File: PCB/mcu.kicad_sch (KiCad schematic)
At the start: 38 parts, among them J2 Conn_Coaxial, J3 Conn_Coaxial, SW2 PTS645VH58-2 LFS, SW3 TS04-66-50-BK-160-SMT, U24 RP2354B, U25 W25Q128JVS, Y1 ABM8AIG-12.000MHZ-12-2Z-T3

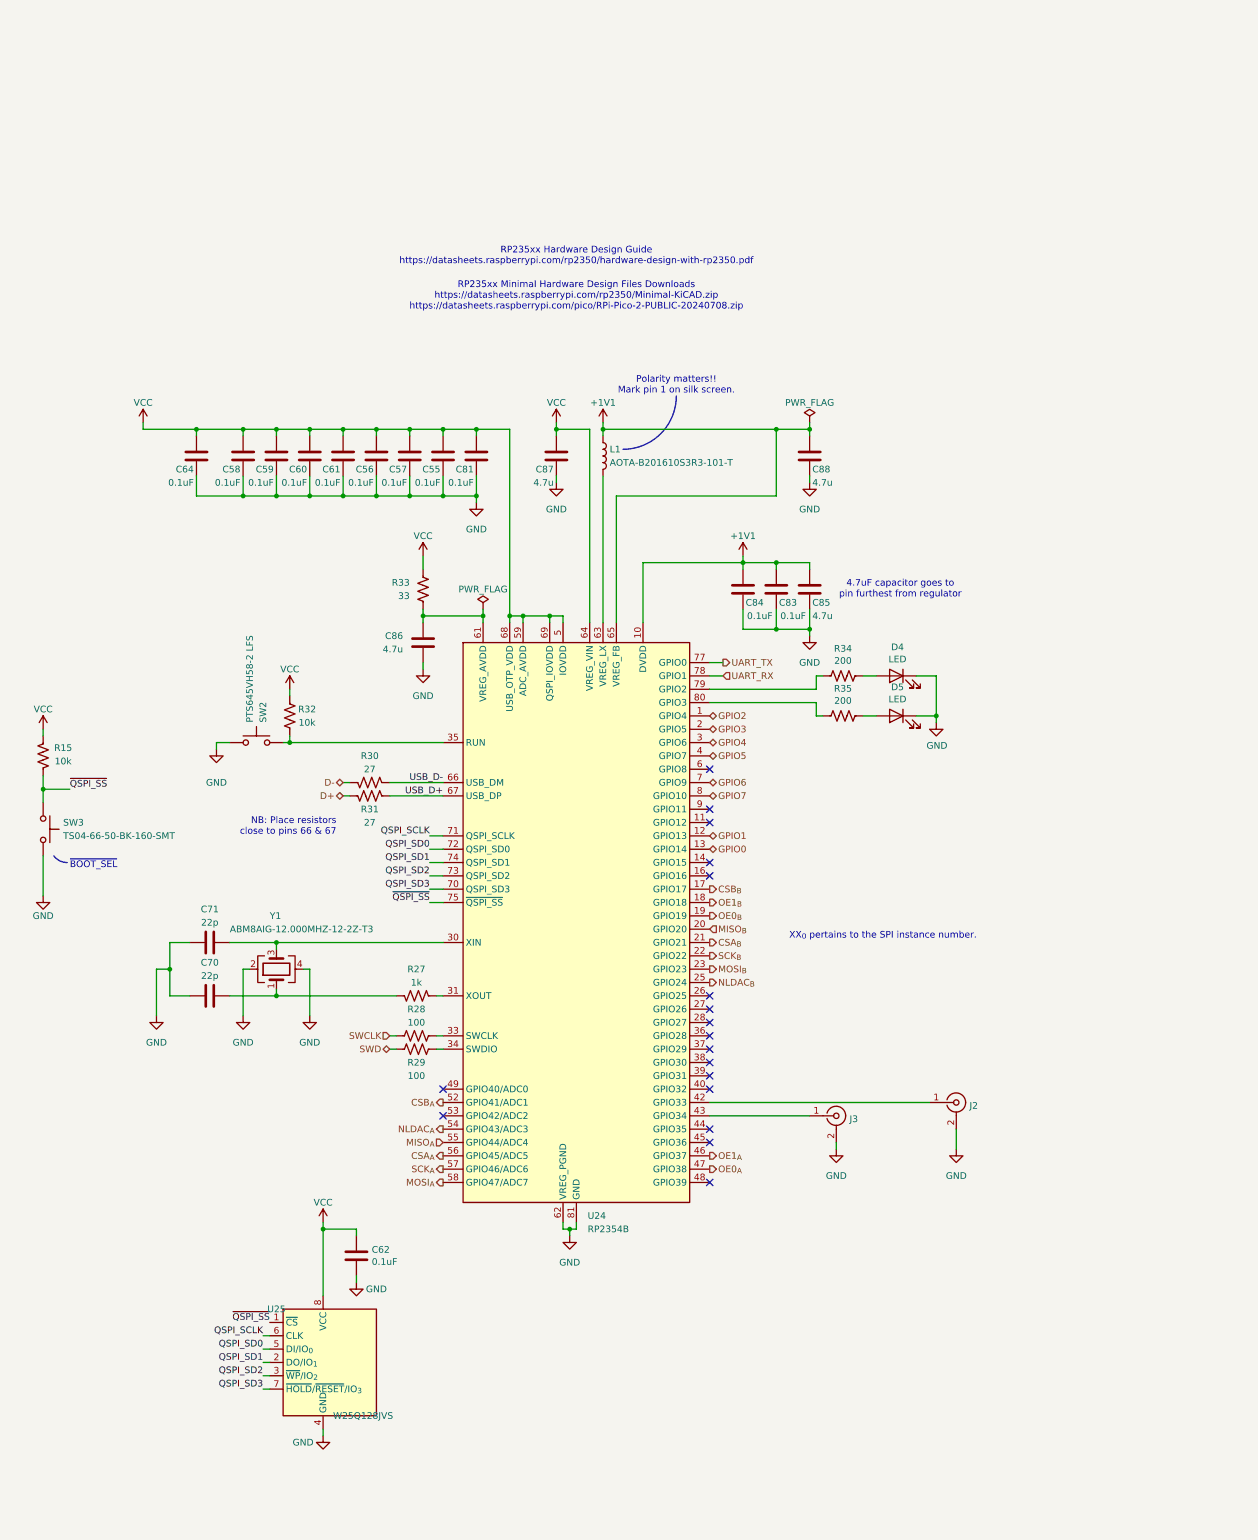
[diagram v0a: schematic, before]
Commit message: Stimjim Rev. B candidate
- Sent to fab
- Lots of manufacturability changes
- BOM consolidation
- Repo layout changed a bit to remove redundant information. e.g.
  datasheet links are embedded in schematic. BOM information embedded in
  schematic. etc
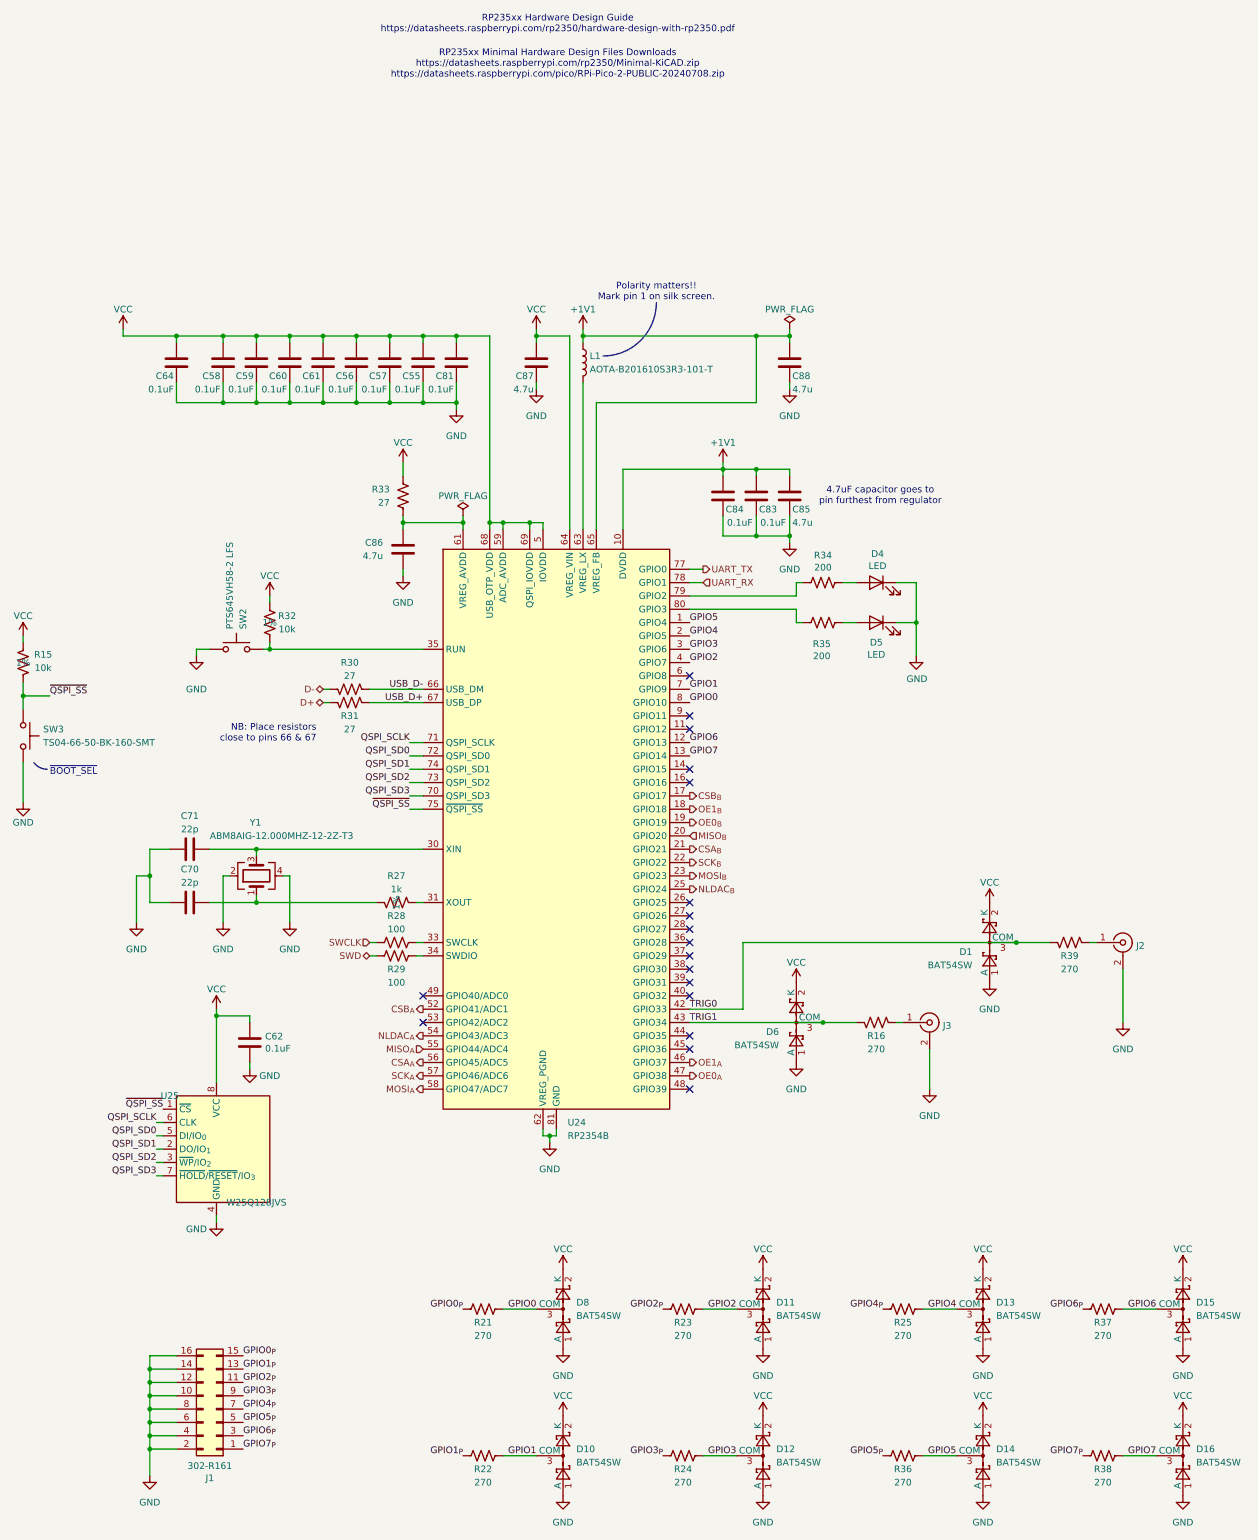
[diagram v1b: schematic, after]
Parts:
- added D1, D10, D11, D12, D13, D14, D15, D16, D6, D8: BAT54SW, Package_TO_SOT_SMD:SOT-323_SC-70, symbol Diode:BAT54SW
- added J1: 302-R161, Connector_IDC:IDC-Header_2x08_P2.54mm_Horizontal, symbol Connector_Generic:Conn_02x08_Odd_Even
- added R16, R21, R22, R23, R24, R25, R36, R37, R38, R39: 270, Resistor_SMD:R_0805_2012Metric, symbol Device:R_US
- C86: Voltage (none) -> 16V
- D4, D5: MPN (none) -> SSF-LXH100GD-01
- J2, J3: value Conn_Coaxial -> 0731375003; MPN (none) -> 0731375003
- L1: MPN (none) -> AOTA-B201610S3R3-101-T
- R15, R27, R28, R29, R32: footprint Resistor_SMD:R_0402_1005Metric -> Resistor_SMD:R_0603_1608Metric; Tolerance (none) -> 1%
- R33: value 33 -> 27
- SW2: MPN (none) -> PTS645VH58-2 LFS
- SW3: MPN (none) -> TS04-66-50-BK-160-SMT
- U24: MPN (none) -> SC1512(13)-A4
- U25: MPN (none) -> W25Q128JVS
- Y1: MPN (none) -> ABM8AIG-12.000MHZ-12-2Z-T3
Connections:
- net GND: now also D1.1 (A), D10.1 (A), D11.1 (A), D12.1 (A), D13.1 (A), D14.1 (A), D15.1 (A), D16.1 (A), D6.1 (A), D8.1 (A), J1.10 (Pin_10), J1.12 (Pin_12), J1.14 (Pin_14), J1.16 (Pin_16), J1.2 (Pin_2), J1.4 (Pin_4), J1.6 (Pin_6), J1.8 (Pin_8)
- net GPIO0: now also U24.8 (GPIO10), D8.3 (COM), R21.2; no longer U24.13 (GPIO14)
- net GPIO1: now also U24.7 (GPIO9), D10.3 (COM), R22.2; no longer U24.12 (GPIO13)
- net GPIO2: now also U24.4 (GPIO7), D11.3 (COM), R23.2; no longer U24.1 (GPIO4)
- net GPIO3: now also U24.3 (GPIO6), D12.3 (COM), R24.2; no longer U24.2 (GPIO5)
- net GPIO4: now also U24.2 (GPIO5), D13.3 (COM), R25.2; no longer U24.3 (GPIO6)
- net GPIO5: now also U24.1 (GPIO4), D14.3 (COM), R36.2; no longer U24.4 (GPIO7)
- net GPIO6: now also U24.12 (GPIO13), D15.3 (COM), R37.2; no longer U24.7 (GPIO9)
- net GPIO7: now also U24.13 (GPIO14), D16.3 (COM), R38.2; no longer U24.8 (GPIO10)
- net VCC: now also D1.2 (K), D10.2 (K), D11.2 (K), D12.2 (K), D13.2 (K), D14.2 (K), D15.2 (K), D16.2 (K), D6.2 (K), D8.2 (K)
- net at J2.1 (In): now also R39.1; no longer U24.42 (GPIO33)
- net at J3.1 (In): now also R16.1; no longer U24.43 (GPIO34)
- new net GPIO0_{P}: J1.15 (Pin_15), R21.1
- new net GPIO1_{P}: J1.13 (Pin_13), R22.1
- new net GPIO2_{P}: J1.11 (Pin_11), R23.1
- new net GPIO3_{P}: J1.9 (Pin_9), R24.1
- new net GPIO4_{P}: J1.7 (Pin_7), R25.1
- new net GPIO5_{P}: J1.5 (Pin_5), R36.1
- new net GPIO6_{P}: J1.3 (Pin_3), R37.1
- new net GPIO7_{P}: J1.1 (Pin_1), R38.1
- new net TRIG0: D1.3 (COM), R39.2, U24.42 (GPIO33)
- new net TRIG1: D6.3 (COM), R16.2, U24.43 (GPIO34)
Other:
- note removed: "XX_{0} pertains to the SPI instance number."
- moved on the sheet: C55, C56, C57, C58, C59, C60, C61, C62, C64, C70, C71, C81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

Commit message: Rev C First Draft
- Fix and move LED footprints
- Move bar code sticker
- Add op-amp unity voltage follower to ADC input
- Remove screw terminals
- Made panel screw holes bigger both panels (3.2mm -> 3.7mm) for 3.4mm
  screws
- Create cutout for mounting rail on panels
- Delete the file with both back and front panels
- Update all footprints (except rp2354b so that its thermal vias pass DRC)
- Add component class and custom rule for USB-C footprint
- Indicate M3 screw in schematic + Add to BOM
- Improve adherence to ADC/DAC datasheets:
  - Move high speed signals out from under ADC (put MISO in +5V layer under ADC)
  - Add 10uF decoupling caps to ADC/DAC
- Change enclosure part number to black enclosure
- Add some more GND vias to isolated GND planes
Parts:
- D4, D5: footprint microstim:LED_D5.0mm_Horizontal_O1.27mm_Z3.0mm_pinSwapped -> open-ephys:LUMEX_SSF-LHXH100GD-01
- SW3: footprint Button_Switch_SMD:SW_SPST_PTS645Sx43SMTR92 -> open-ephys:SAMESKY_TS04-66-XX-BK-XXX-SMT-XX
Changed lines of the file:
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@@
 			)
 		)
-		(property "Footprint" "microstim:LED_D5.0mm_Horizontal_O1.27mm_Z3.0mm_pinSwapped"
+		(property "Footprint" "open-ephys:LUMEX_SSF-LHXH100GD-01"
 			(at 196.85 88.9 0)
 			(effects
@@
 			)
 		)
-		(property "Footprint" "microstim:LED_D5.0mm_Horizontal_O1.27mm_Z3.0mm_pinSwapped"
+		(property "Footprint" "open-ephys:LUMEX_SSF-LHXH100GD-01"
 			(at 196.85 96.52 0)
 			(effects
@@
 			)
 		)
-		(property "Footprint" "Button_Switch_SMD:SW_SPST_PTS645Sx43SMTR92"
+		(property "Footprint" "open-ephys:SAMESKY_TS04-66-XX-BK-XXX-SMT-XX"
 			(at 39.37 118.11 0)
 			(effects
